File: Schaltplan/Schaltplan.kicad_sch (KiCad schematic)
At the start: 16 parts, among them J1 Conn_01x02_Pin, J2 Conn_01x02_Pin, Q1 IRLZ44N, Q2 IRLZ44N, U1 ACS712xLCTR-05B

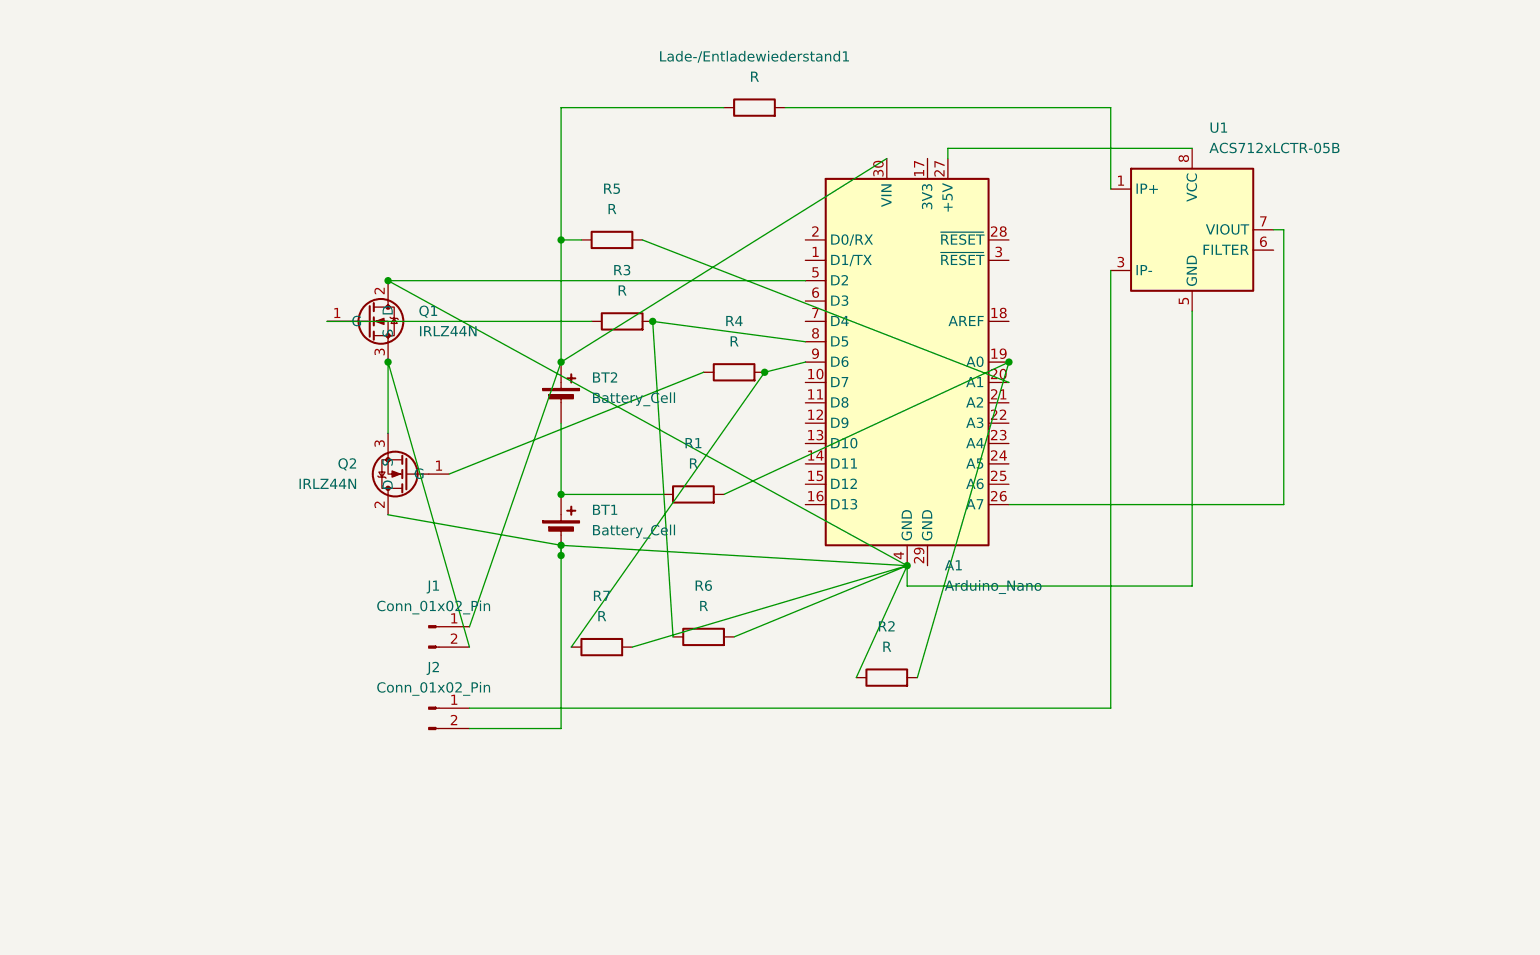
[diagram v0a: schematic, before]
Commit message: Update junctions and wires in schematic for improved layout
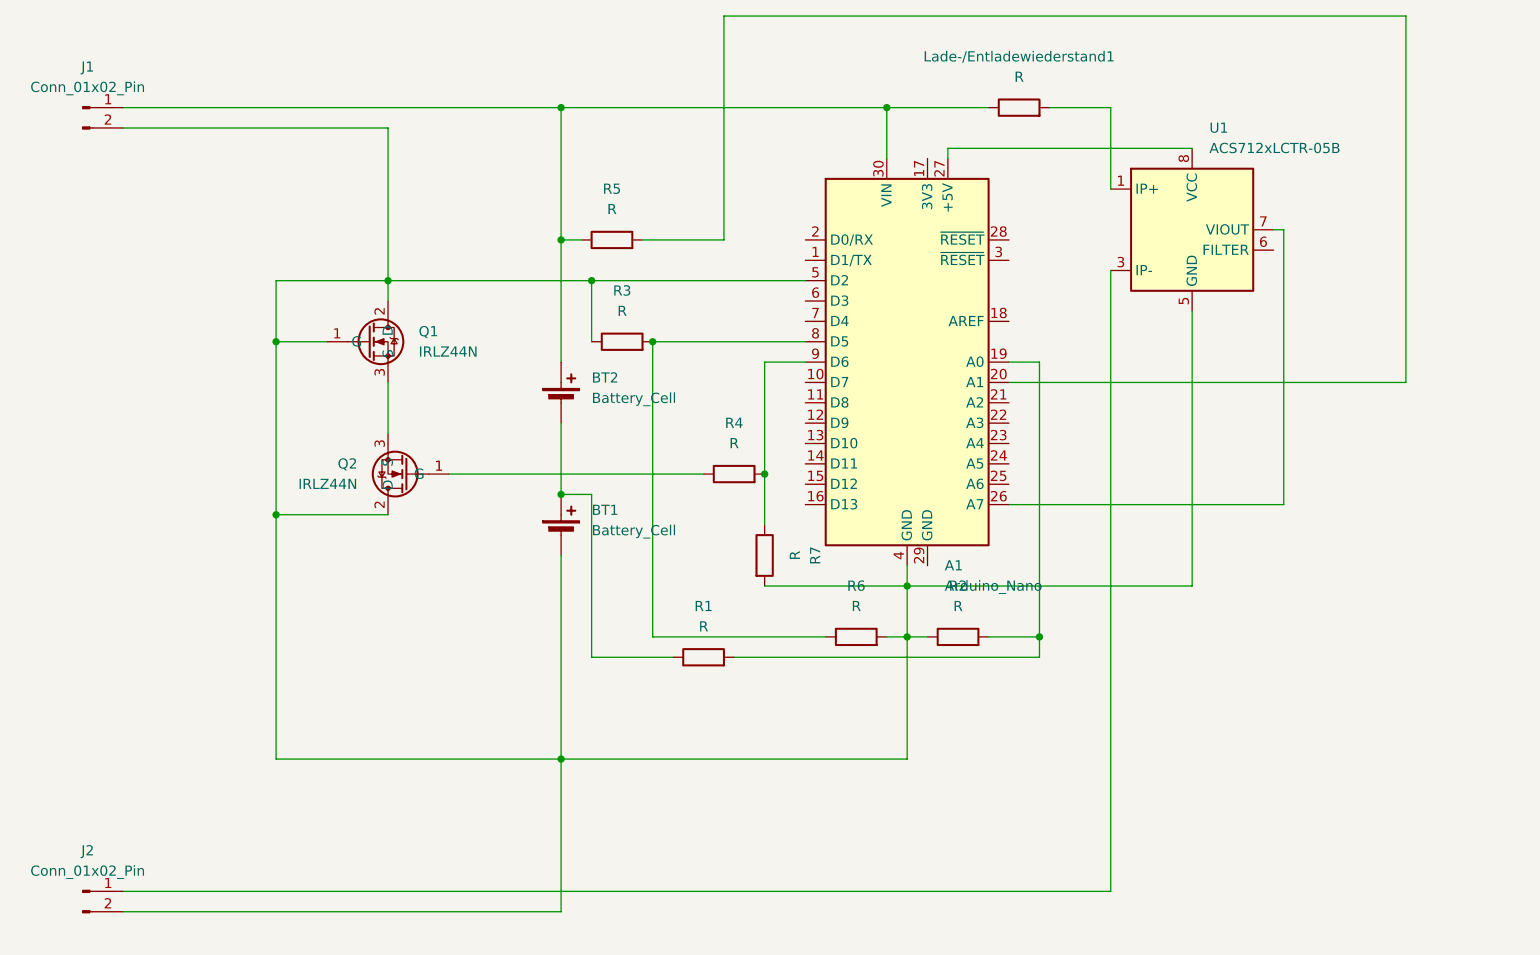
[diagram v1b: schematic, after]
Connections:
- net at A1.4 (GND), A1.5 (D2), BT1.2 (-)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: now also J1.2 (Pin_2), Q1.1 (G), R3.1
- net at Q1.3 (S), Q2.3 (S): no longer J1.2 (Pin_2)
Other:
- moved on the sheet: J1, J2, Lade-/Entladewiederstand1, Q1, R1, R2, R3, R4, R6, R7

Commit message: Add new components: LM2577 DC-DC Step-Up Module, LED, and Battery Cells to schematic
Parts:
- added BT3, BT4: Battery_Cell, symbol Device:Battery_Cell
- added D1: LED, symbol Device:LED
- added J3: LM2577 DC-DC Step-Up Modul, symbol Connector_Generic:Conn_01x04
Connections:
- net at A1.4 (GND), A1.5 (D2), BT1.2 (-)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: now also BT4.2 (-), J3.2 (IN-); no longer J2.2 (Pin_2)
- net at U1.3 (IP-), U1.4 (IP-): now also J3.1 (IN+); no longer J2.1 (Pin_1)
- net at A1.27 (+5V), U1.8 (VCC): now also BT3.1 (+)
- new net: BT3.2 (-), D1.2 (A)
- new net: J2.1 (Pin_1), J3.3 (OUT+)
- new net: J2.2 (Pin_2), J3.4 (Pin_4)
- new net: BT4.1 (+), D1.1 (K)
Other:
- moved on the sheet: R4
